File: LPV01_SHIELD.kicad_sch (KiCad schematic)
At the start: 123 parts, among them J1 Screw_Terminal_01x02, J10 SPI_header, J11 Power_socket, J15 Inputs, J16 Screw_Terminal_01x02, J17 Wiegand, J2 Screw_Terminal_01x02, J22 Inputs, J23 Screw_Terminal_01x02, J24 Conn_01x02_Pin, J3 Screw_Terminal_01x02, J9 GPIO_header, Q1 BC817, Q10 BC817, Q11 BC817, Q12 BC817, Q13 BC817, Q14 BC817, Q15 BC817, Q2 BC817, Q3 BC817, Q4 TLP521-4XSM, Q5 TLP521-4XSM, Q6 TLP521-4XSM, Q7 BC817, Q8 TLP521-4XSM, Q9 BC817, SW1 SW_SPST, SW10 SW_SPST, SW11 SW_SPST, SW2 SW_SPST, SW3 SW_SPST, SW4 SW_SPST, SW5 SW_SPST, SW6 SW_SPST, SW7 SW_SPST, SW8 SW_SPST, SW9 SW_SPST, U1 TLP175A, U2 TLP175A, U3 TLP175A

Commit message: PCB rebuilt
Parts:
- removed D10, D12, D14, D8: LED, symbol Device:LED
- removed D18, D20, D22, D24, D26, D28, D29: LED, LED_SMD:LED_0603_1608Metric, symbol Device:LED
- removed D2, D4, D6: SMF48CA, Diode_SMD:D_SMA, symbol Diode:SD36_SOD323
- removed D21, D23, D25, D27, D30, D31: D, symbol Device:D
- removed J1, J2, J3: Screw_Terminal_01x02, TerminalBlock_Phoenix:TerminalBlock_Phoenix_MKDS-1,5-2_1x02_P5.00mm_Horizontal, symbol Connector:Screw_Terminal_01x02
- removed J15: Inputs, TerminalBlock_Phoenix:TerminalBlock_Phoenix_PT-1,5-8-3.5-H_1x08_P3.50mm_Horizontal, symbol Connector:Screw_Terminal_01x08
- removed J16: Screw_Terminal_01x02, TerminalBlock_Phoenix:TerminalBlock_Phoenix_PT-1,5-2-3.5-H_1x02_P3.50mm_Horizontal, symbol Connector:Screw_Terminal_01x02
- removed Q1, Q10, Q11, Q12, Q13, Q14, Q15: BC817, Package_TO_SOT_SMD:SOT-23, symbol Transistor_BJT:BC817
- removed Q4, Q5, Q6, Q8: TLP521-4XSM, SamacSys_Parts:TLP5214XSM, symbol SamacSys_Parts:TLP521-4XSM
- removed R10: 4k7, Resistor_SMD:R_0603_1608Metric, symbol Device:R
- removed R34, R35: 2k2, Resistor_SMD:R_0603_1608Metric, symbol Device:R
- removed R36, R38, R39, R40, R41, R42, R43, R44, R45, R46, R47: 10k, Resistor_SMD:R_0603_1608Metric, symbol Device:R
- removed R37: 10k ->, Resistor_SMD:R_0603_1608Metric, symbol Device:R
- removed R48, R49, R50, R51, R52, R53, R54, R55, R56, R58, R59, R60, R61, R62, R63: 1k, Resistor_SMD:R_0603_1608Metric, symbol Device:R
- removed SW10, SW11, SW9: SW_SPST, Button_Switch_SMD:SW_SPST_CK_RS282G05A3, symbol Switch:SW_SPST
- removed U1, U2, U3: TLP175A, Package_SO:MFSOP6-4_4.4x3.6mm_P1.27mm, symbol Relay_SolidState:TLP175A
- added D10, D12, D14, D4, D6, D8: D, Diode_SMD:D_MicroMELF, symbol Device:D
- added D9: LED, LED_SMD:LED_0603_1608Metric, symbol Device:LED
- added J6: Relay_PWR, TerminalBlock_Phoenix:TerminalBlock_Phoenix_PT-1,5-2-3.5-H_1x02_P3.50mm_Horizontal, symbol Connector:Screw_Terminal_01x02
- added Q101, Q102: TLP521-4XSM, SamacSys_Parts:TLP5214XSM, symbol SamacSys_Parts:TLP521-4XSM
- added Q4, Q5, Q6, Q8: BC817, Package_TO_SOT_SMD:SOT-23, symbol Transistor_BJT:BC817
- added R17, R20, R23, R26: 2k2, Resistor_SMD:R_0603_1608Metric, symbol Device:R
- added R18, R21, R24, R27: 22k, Resistor_SMD:R_0603_1608Metric, symbol Device:R
- added R19, R22, R25: 4k7, Resistor_SMD:R_0603_1608Metric, symbol Device:R
- D11, D13, D15, D7: footprint (none) -> LED_SMD:LED_0603_1608Metric
- D16: footprint (none) -> Diode_SMD:D_MicroMELF
- D17: value LED -> STATUS
- D2: renamed from D19; footprint (none) -> Diode_SMD:D_MicroMELF
- J2: renamed from J11; value Power_socket -> PWR_socket
- J4: renamed from J23; value Screw_Terminal_01x02 -> Relay_PWR_in
- J5: renamed from J24; footprint (none) -> Connector_PinHeader_2.54mm:PinHeader_1x02_P2.54mm_Vertical
- R1, R5: value 1k -> 470R
- R10: renamed from R57; value 1k -> 4k7
- R11: value 4k7 -> 2k2
- R12, R15: value 10k -> 22k
- R13, R16, R28: value 10k -> 4k7
- R2, R3, R6, R7: value 4k7 -> 470R
- R30: value 2k2 -> 22k
- R31: value 2k2 -> 4k7
- R33: value 2k2 -> 1k
- R4, R8: value 10k -> 470R
- R9: value 1k -> 22k
- renumbered J9 to J1, J10 to J3, J17 to J7, J22 to J8, Q9 to Q1
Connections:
- net +24V: no longer R14.2, R29.2, R30.2, R31.2, R32.2, R33.2
- net +5V: now also SW1.2 (B), SW2.2 (B), SW3.2 (B), SW4.2 (B), SW5.2 (B), SW6.2 (B), SW7.2 (B), SW8.2 (B), Q101.10 (C_1), Q101.12 (C_2), Q101.14 (C_3), Q101.16 (C_4), Q102.10 (C_1), Q102.12 (C_2), Q102.14 (C_3), Q102.16 (C_4); no longer R1.2, R13.1, R15.1, R16.1, R2.2, R28.1, R5.2, R6.2, R9.2, SW4.1 (A), SW5.1 (A), SW6.1 (A), SW7.1 (A), SW8.1 (A)
- net D10: now also R1.2
- net D11: now also R2.2
- net D12: now also R3.2
- net D13: now also D17.2 (A)
- net D18: now also R5.2
- net D19: now also R6.2
- net D2: no longer R13.2
- net D21: now also R4.2
- net D22: now also R7.2
- net D23: now also R8.2
- net D3: no longer R15.2
- net D4: no longer R16.2
- net D5: no longer R28.2
- net GND: now also R15.2, R30.2, R33.1, R9.2, Q101.2 (K_1), Q101.4 (K_2), Q101.6 (K_3), Q101.8 (K_4), Q102.2 (K_1), Q102.4 (K_2), Q102.6 (K_3), Q102.8 (K_4), Q4.2 (E), Q5.2 (E), Q6.2 (E), Q8.2 (E), R18.2, R21.2, R24.2, R27.2; no longer R4.2, R8.2, SW1.2 (B), SW2.2 (B), SW3.2 (B)
- net MISO: no longer R3.1
- net MOSI: no longer R11.1
- net O1: now also R10.1, R9.1, SW1.1 (A), Q101.15 (E_4); no longer D17.2 (A), SW4.2 (B), SW5.2 (B), SW6.2 (B), SW7.2 (B), SW8.2 (B)
- net O2: now also R12.1, R13.1, SW2.1 (A), Q101.13 (E_3)
- net O3: now also R15.1, R16.1, SW3.1 (A), Q101.11 (E_2)
- net O4: now also SW4.1 (A), Q101.9 (E_1), R18.1, R19.1
- net O5: now also SW5.1 (A), Q102.15 (E_4), R21.1, R22.1
- net O6: now also SW6.1 (A), Q102.13 (E_3), R24.1, R25.1
- net O7: now also R28.1, SW7.1 (A), Q102.11 (E_2), R27.1
- net O8: now also R30.1, R31.1, SW8.1 (A), Q102.9 (E_1)
- net OUT1: now also D1.1 (K), D2.2 (A), Q1.3 (C); no longer D16.2 (A), Q7.3 (C)
- net OUT2: now also D3.1 (K), Q2.3 (C), D4.2 (A); no longer D2.2 (A), Q1.3 (C)
- net OUT3: now also D5.1 (K), Q3.3 (C), D6.2 (A)
- net OUT4: now also D7.1 (K), D8.2 (A), Q4.3 (C)
- net OUT5: now also D10.2 (A), D9.1 (K), Q5.3 (C)
- net OUT6: now also D11.1 (K), D12.2 (A), Q6.3 (C)
- net OUT7: now also D13.1 (K), Q7.3 (C), D14.2 (A)
- net OUT8: now also D15.1 (K), D16.2 (A), Q8.3 (C)
- net SCK: no longer R7.1
- net VR: now also R11.1, R14.1, R29.1, R32.1, D10.1 (K), D12.1 (K), D14.1 (K), D4.1 (K), D6.1 (K), D8.1 (K), J6.1 (Pin_1), J6.2 (Pin_2), R17.1, R20.1, R23.1, R26.1
- net at R4.1: now also Q101.7 (A_4); no longer R3.2
- net at Q7.1 (B): now also R28.2
- net at D15.2 (A): now also R32.2
- net at D17.1 (K): now also R33.2
- net at D11.2 (A): now also R26.2; no longer R30.1
- net at D5.2 (A): now also R17.2
- net at R6.1: now also Q102.3 (A_2); no longer D3.2 (A)
- net at R5.1: now also Q102.1 (A_1)
- net at R1.1: now also Q101.1 (A_1)
- net at D13.2 (A): now also R29.2; no longer R33.1
- net at D7.2 (A): now also R20.2; no longer R14.1
- net at R2.1: now also Q101.3 (A_2); no longer D1.2 (A)
- new net: Q6.1 (B), R25.2
- new net: Q8.1 (B), R31.2
- new net: D9.2 (A), R23.2
- new net: Q4.1 (B), R19.2
- new net: Q5.1 (B), R22.2
- new net: Q102.7 (A_4), R8.1
- new net: Q3.1 (B), R16.2
- new net: D1.2 (A), R11.2
- new net: Q101.5 (A_3), R3.1
- new net: Q102.5 (A_3), R7.1
- new net: D3.2 (A), R14.2
- new net: Q2.1 (B), R13.2
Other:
- removed sheet USART
- removed sheet USB_hub
- added sheet Inputs (inputs.kicad_sch)
- moved on the sheet: D2, J1, J2, J3, J4, J5, J7, J8, Q1, R10

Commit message: First traces added
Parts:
- added H1, H2, H3, H4: MountingHole, MountingHole:MountingHole_3.2mm_M3_DIN965_Pad, symbol Mechanical:MountingHole
- D10, D12, D14, D16, D2, D4, D6, D8: footprint Diode_SMD:D_MicroMELF -> Diode_SMD:D_SMA
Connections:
- net +5V: now also Q101.11 (E_2), Q101.13 (E_3), Q101.15 (E_4), Q101.9 (E_1), Q102.11 (E_2), Q102.13 (E_3), Q102.15 (E_4), Q102.9 (E_1); no longer Q101.10 (C_1), Q101.12 (C_2), Q101.14 (C_3), Q101.16 (C_4), Q102.10 (C_1), Q102.12 (C_2), Q102.14 (C_3), Q102.16 (C_4)
- net D10: no longer R1.2
- net D11: no longer R2.2
- net D12: no longer R3.2
- net D18: no longer R5.2
- net D19: no longer R6.2
- net D21: no longer R4.2
- net D22: no longer R7.2
- net D23: no longer R8.2
- net GND: now also Q101.1 (A_1), Q101.3 (A_2), Q101.5 (A_3), Q101.7 (A_4), Q102.1 (A_1), Q102.3 (A_2), Q102.5 (A_3), Q102.7 (A_4); no longer Q101.2 (K_1), Q101.4 (K_2), Q101.6 (K_3), Q101.8 (K_4), Q102.2 (K_1), Q102.4 (K_2), Q102.6 (K_3), Q102.8 (K_4)
- net O1: now also Q101.10 (C_1); no longer Q101.15 (E_4)
- net O2: now also Q101.12 (C_2); no longer Q101.13 (E_3)
- net O3: now also Q101.14 (C_3); no longer Q101.11 (E_2)
- net O4: now also Q101.16 (C_4); no longer Q101.9 (E_1)
- net O5: now also Q102.10 (C_1); no longer Q102.15 (E_4)
- net O6: now also Q102.12 (C_2); no longer Q102.13 (E_3)
- net O7: now also Q102.14 (C_3); no longer Q102.11 (E_2)
- net O8: now also Q102.16 (C_4); no longer Q102.9 (E_1)
- net at R6.1: now also Q102.6 (K_3); no longer Q102.3 (A_2)
- net at R8.1: now also Q102.2 (K_1); no longer Q102.7 (A_4)
- net at R2.1: now also Q101.6 (K_3); no longer Q101.3 (A_2)
- net at R3.1: now also Q101.4 (K_2); no longer Q101.5 (A_3)
- net at R7.1: now also Q102.4 (K_2); no longer Q102.5 (A_3)
- net at R4.1: now also Q101.2 (K_1); no longer Q101.7 (A_4)
- net at R5.1: now also Q102.8 (K_4); no longer Q102.1 (A_1)
- net at R1.1: now also Q101.8 (K_4); no longer Q101.1 (A_1)

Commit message: More traces + components alignment
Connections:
- net +5V: now also Q101.10 (C_1), Q101.12 (C_2), Q101.14 (C_3), Q101.16 (C_4), Q102.10 (C_1), Q102.12 (C_2), Q102.14 (C_3), Q102.16 (C_4); no longer Q101.11 (E_2), Q101.13 (E_3), Q101.15 (E_4), Q101.9 (E_1), Q102.11 (E_2), Q102.13 (E_3), Q102.15 (E_4), Q102.9 (E_1)
- net D10: now also R5.2
- net D11: now also R7.2
- net D2: now also R2.2
- net D3: now also R4.2
- net D4: now also R6.2
- net D5: now also R8.2
- net D8: now also R1.2
- net D9: now also R3.2
- net GND: now also Q101.2 (K_1), Q101.4 (K_2), Q101.6 (K_3), Q101.8 (K_4), Q102.2 (K_1), Q102.4 (K_2), Q102.6 (K_3), Q102.8 (K_4); no longer Q101.1 (A_1), Q101.3 (A_2), Q101.5 (A_3), Q101.7 (A_4), Q102.1 (A_1), Q102.3 (A_2), Q102.5 (A_3), Q102.7 (A_4)
- net O1: now also Q101.15 (E_4); no longer Q101.10 (C_1)
- net O2: now also Q101.13 (E_3); no longer Q101.12 (C_2)
- net O3: now also Q101.11 (E_2); no longer Q101.14 (C_3)
- net O4: now also Q101.9 (E_1); no longer Q101.16 (C_4)
- net O5: now also Q102.15 (E_4); no longer Q102.10 (C_1)
- net O6: now also Q102.13 (E_3); no longer Q102.12 (C_2)
- net O7: now also Q102.11 (E_2); no longer Q102.14 (C_3)
- net O8: now also Q102.9 (E_1); no longer Q102.16 (C_4)
- net at R6.1: now also Q102.3 (A_2); no longer Q102.6 (K_3)
- net at R8.1: now also Q102.7 (A_4); no longer Q102.2 (K_1)
- net at R2.1: now also Q101.3 (A_2); no longer Q101.6 (K_3)
- net at R3.1: now also Q101.5 (A_3); no longer Q101.4 (K_2)
- net at R7.1: now also Q102.5 (A_3); no longer Q102.4 (K_2)
- net at R4.1: now also Q101.7 (A_4); no longer Q101.2 (K_1)
- net at R5.1: now also Q102.1 (A_1); no longer Q102.8 (K_4)
- net at R1.1: now also Q101.1 (A_1); no longer Q101.8 (K_4)
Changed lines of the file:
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@@
 		)
 	)
-	(global_label "D23"
+	(global_label "D9"
 		(shape input)
-		(at 21.59 73.66 180)
+		(at 22.86 36.83 180)
 		(fields_autoplaced yes)
 		(effects
@@
 		)
 		(property "Intersheetrefs" "${INTERSHEET_REFS}"
-			(at 14.9158 73.66 0)
+			(at 17.3953 36.83 0)
 			(effects
 				(font
@@
 		)
 	)
-	(global_label "D18"
+	(global_label "D4"
 		(shape input)
-		(at 21.59 58.42 180)
+		(at 22.86 63.5 180)
 		(fields_autoplaced yes)
 		(effects
@@
 		)
 		(property "Intersheetrefs" "${INTERSHEET_REFS}"
-			(at 14.9158 58.42 0)
+			(at 17.3953 63.5 0)
 			(effects
 				(font
@@
 		)
 	)
-	(global_label "D11"
+	(global_label "D8"
 		(shape input)
-		(at 21.59 31.75 180)
+		(at 22.86 26.67 180)
 		(fields_autoplaced yes)
 		(effects
@@
 		)
 		(property "Intersheetrefs" "${INTERSHEET_REFS}"
-			(at 14.9158 31.75 0)
+			(at 17.3953 26.67 0)
 			(effects
 				(font
@@
 		)
 	)
-	(global_label "D22"
+	(global_label "D5"
 		(shape input)
-		(at 21.59 68.58 180)
+		(at 22.86 73.66 180)
 		(fields_autoplaced yes)
 		(effects
@@
 		)
 		(property "Intersheetrefs" "${INTERSHEET_REFS}"
-			(at 14.9158 68.58 0)
+			(at 17.3953 73.66 0)
 			(effects
 				(font
@@
 		)
 	)
-	(global_label "D12"
+	(global_label "D3"
 		(shape input)
-		(at 21.59 36.83 180)
+		(at 22.86 41.91 180)
 		(fields_autoplaced yes)
 		(effects
@@
 		)
 		(property "Intersheetrefs" "${INTERSHEET_REFS}"
-			(at 14.9158 36.83 0)
+			(at 17.3953 41.91 0)
 			(effects
 				(font
@@
 		)
 	)
-	(global_label "D19"
+	(global_label "D11"
 		(shape input)
-		(at 21.59 63.5 180)
+		(at 22.86 68.58 180)
 		(fields_autoplaced yes)
 		(effects
@@
 		)
 		(property "Intersheetrefs" "${INTERSHEET_REFS}"
-			(at 14.9158 63.5 0)
+			(at 16.1858 68.58 0)
 			(effects
 				(font
@@
 		)
 	)
-	(global_label "D10"
+	(global_label "D2"
 		(shape input)
-		(at 21.59 26.67 180)
+		(at 22.86 31.75 180)
 		(fields_autoplaced yes)
 		(effects
@@
 		)
 		(property "Intersheetrefs" "${INTERSHEET_REFS}"
-			(at 14.9158 26.67 0)
+			(at 17.3953 31.75 0)
 			(effects
 				(font
@@
 		)
 	)
-	(global_label "D21"
+	(global_label "D10"
 		(shape input)
-		(at 21.59 41.91 180)
+		(at 22.86 58.42 180)
 		(fields_autoplaced yes)
 		(effects
@@
 		)
 		(property "Intersheetrefs" "${INTERSHEET_REFS}"
-			(at 14.9158 41.91 0)
+			(at 16.1858 58.42 0)
 			(effects
 				(font
@@
 	(symbol
 		(lib_id "SamacSys_Parts:TLP521-4XSM")
-		(at 41.91 76.2 0)
-		(mirror x)
+		(at 41.91 58.42 0)
 		(unit 1)
 		(exclude_from_sim no)
@@
 		(dnp no)
 		(property "Reference" "Q102"
-			(at 55.118 51.816 0)
+			(at 55.118 52.07 0)
 			(effects
 				(font
@@
 		)
 		(property "Value" "TLP521-4XSM"
-			(at 54.61 54.356 0)
+			(at 54.864 54.61 0)
 			(effects
 				(font
@@
 		)
 		(property "Footprint" "SamacSys_Parts:TLP5214XSM"
-			(at 63.5 78.74 0)
+			(at 63.5 55.88 0)
 			(effects
 				(font
@@
 		)
 		(property "Datasheet" "http://isocom.com/wp-content/uploads/2018/03/dd93208-small-tlp521-1_2-4-240817.pdf"
-			(at 63.5 76.2 0)
+			(at 63.5 58.42 0)
 			(effects
 				(font
@@
 		)
 		(property "Description" "OPTOISO 5.3KV 4CH TRANS 16SMD"
-			(at 41.91 76.2 0)
+			(at 41.91 58.42 0)
 			(effects
 				(font
@@
 		)
 		(property "Description_1" "OPTOISO 5.3KV 4CH TRANS 16SMD"
-			(at 63.5 73.66 0)
+			(at 63.5 60.96 0)
 			(effects
 				(font
@@
 		)
 		(property "Height" "4.6"
-			(at 63.5 71.12 0)
+			(at 63.5 63.5 0)
 			(effects
 				(font
@@
 		)
 		(property "Manufacturer_Name" "Isocom"
-			(at 63.5 68.58 0)
+			(at 63.5 66.04 0)
 			(effects
 				(font
@@
 		)
 		(property "Manufacturer_Part_Number" "TLP521-4XSM"
-			(at 63.5 66.04 0)
+			(at 63.5 68.58 0)
 			(effects
 				(font
@@
 		)
 		(property "Mouser Part Number" ""
-			(at 63.5 63.5 0)
+			(at 63.5 71.12 0)
 			(effects
 				(font
@@
 		)
 		(property "Mouser Price/Stock" ""
-			(at 63.5 60.96 0)
+			(at 63.5 73.66 0)
 			(effects
 				(font
@@
 		)
 		(property "Arrow Part Number" ""
-			(at 63.5 58.42 0)
+			(at 63.5 76.2 0)
 			(effects
 				(font
@@
 		)
 		(property "Arrow Price/Stock" ""
-			(at 63.5 55.88 0)
+			(at 63.5 78.74 0)
 			(effects
 				(font
@@
 	(symbol
 		(lib_id "SamacSys_Parts:TLP521-4XSM")
-		(at 41.91 44.45 0)
-		(mirror x)
+		(at 41.91 26.67 0)
 		(unit 1)
 		(exclude_from_sim no)
@@
 		)
 		(property "Value" "TLP521-4XSM"
-			(at 54.356 22.098 0)
+			(at 54.864 22.352 0)
 			(effects
 				(font
@@
 		)
 		(property "Footprint" "SamacSys_Parts:TLP5214XSM"
-			(at 63.5 46.99 0)
+			(at 63.5 24.13 0)
 			(effects
 				(font
@@
 		)
 		(property "Datasheet" "http://isocom.com/wp-content/uploads/2018/03/dd93208-small-tlp521-1_2-4-240817.pdf"
-			(at 63.5 44.45 0)
+			(at 63.5 26.67 0)
 			(effects
 				(font
@@
 		)
 		(property "Description" "OPTOISO 5.3KV 4CH TRANS 16SMD"
-			(at 41.91 44.45 0)
+			(at 41.91 26.67 0)
 			(effects
 				(font
@@
 		)
 		(property "Description_1" "OPTOISO 5.3KV 4CH TRANS 16SMD"
-			(at 63.5 41.91 0)
+			(at 63.5 29.21 0)
 			(effects
 				(font
@@
 		)
 		(property "Height" "4.6"
-			(at 63.5 39.37 0)
+			(at 63.5 31.75 0)
 			(effects
 				(font
@@
 		)
 		(property "Manufacturer_Name" "Isocom"
-			(at 63.5 36.83 0)
+			(at 63.5 34.29 0)
 			(effects
 				(font
@@
 		)
 		(property "Manufacturer_Part_Number" "TLP521-4XSM"
-			(at 63.5 34.29 0)
+			(at 63.5 36.83 0)
 			(effects
 				(font
@@
 		)
 		(property "Mouser Part Number" ""
-			(at 63.5 31.75 0)
+			(at 63.5 39.37 0)
 			(effects
 				(font
@@
 		)
 		(property "Mouser Price/Stock" ""
-			(at 63.5 29.21 0)
+			(at 63.5 41.91 0)
 			(effects
 				(font
@@
 		)
 		(property "Arrow Part Number" ""
-			(at 63.5 26.67 0)
+			(at 63.5 44.45 0)
 			(effects
 				(font
@@
 		)
 		(property "Arrow Price/Stock" ""
-			(at 63.5 24.13 0)
+			(at 63.5 46.99 0)
 			(effects
 				(font

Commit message: Made the PCK the size of the LP board
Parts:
- removed Q101, Q102: TLP521-4XSM, SamacSys_Parts:TLP5214XSM, symbol SamacSys_Parts:TLP521-4XSM
- removed SW1, SW2, SW3, SW4, SW5, SW6, SW7, SW8: SW_SPST, Button_Switch_SMD:SW_SPST_CK_RS282G05A3, symbol Switch:SW_SPST
- added U2, U3: TCMT4100, Package_SO:SOP-16_4.4x10.4mm_P1.27mm, symbol Isolator:TCMT4100
- H1, H2, H3, H4: footprint MountingHole:MountingHole_3.2mm_M3_DIN965_Pad -> MountingHole:MountingHole_3.2mm_M3_DIN965
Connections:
- net +5V: now also U2.10, U2.12, U2.14, U2.16, U3.10, U3.12, U3.14, U3.16
- net GND: now also U2.2, U2.4, U2.6, U2.8, U3.2, U3.4, U3.6, U3.8
- net O1: now also U2.15
- net O2: now also U2.13
- net O3: now also U2.11
- net O4: now also U2.9
- net O5: now also U3.15
- net O6: now also U3.13
- net O7: now also U3.11
- net O8: now also U3.9
- net at R6.1: now also U3.3
- net at R8.1: now also U3.7
- net at R2.1: now also U2.3
- net at R3.1: now also U2.5
- net at R7.1: now also U3.5
- net at R4.1: now also U2.7
- net at R5.1: now also U3.1
- net at R1.1: now also U2.1
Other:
- moved on the sheet: D17, H1, H2, H3, H4, J1, J2, J3, J4, J5, J6, J7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

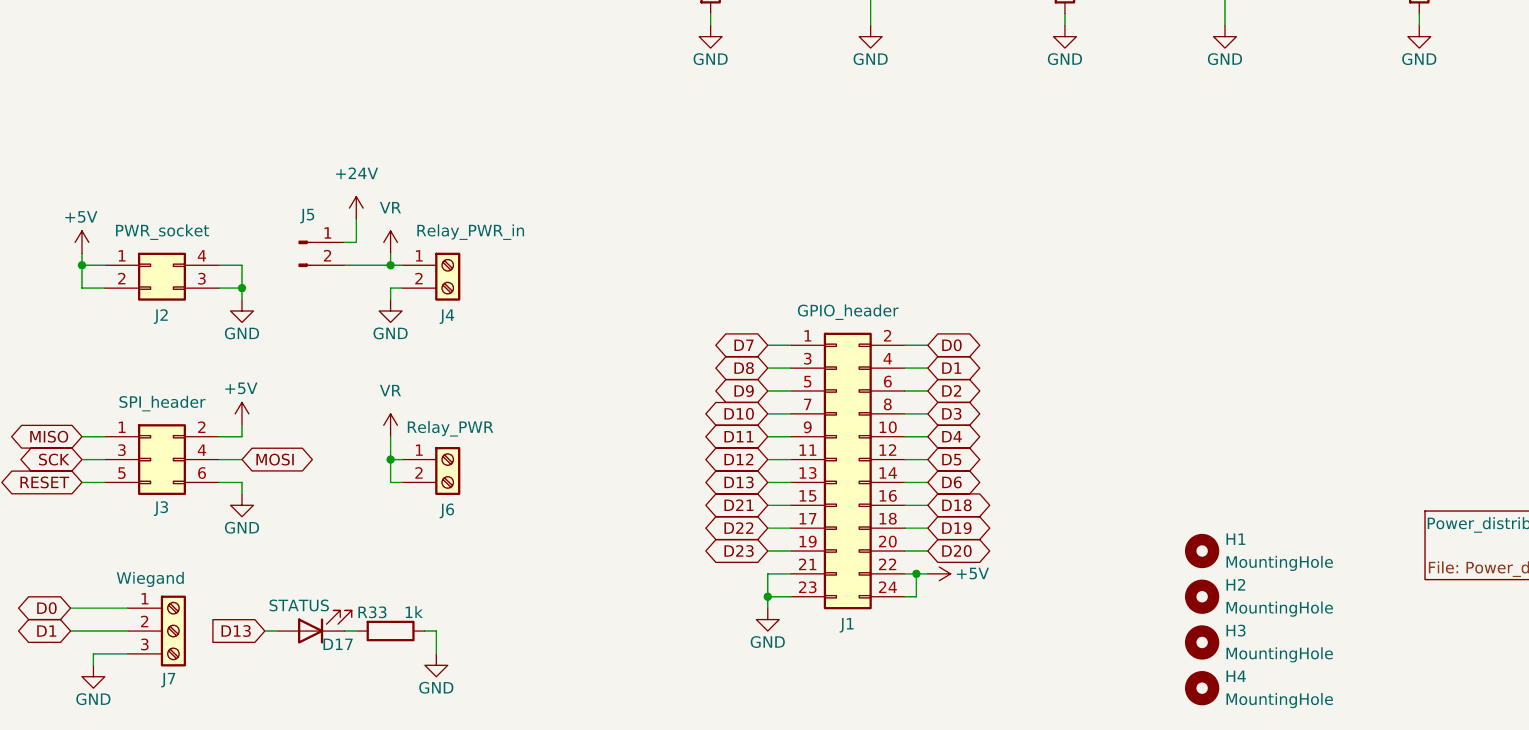
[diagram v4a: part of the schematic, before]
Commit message: PCB shortened to final measurements
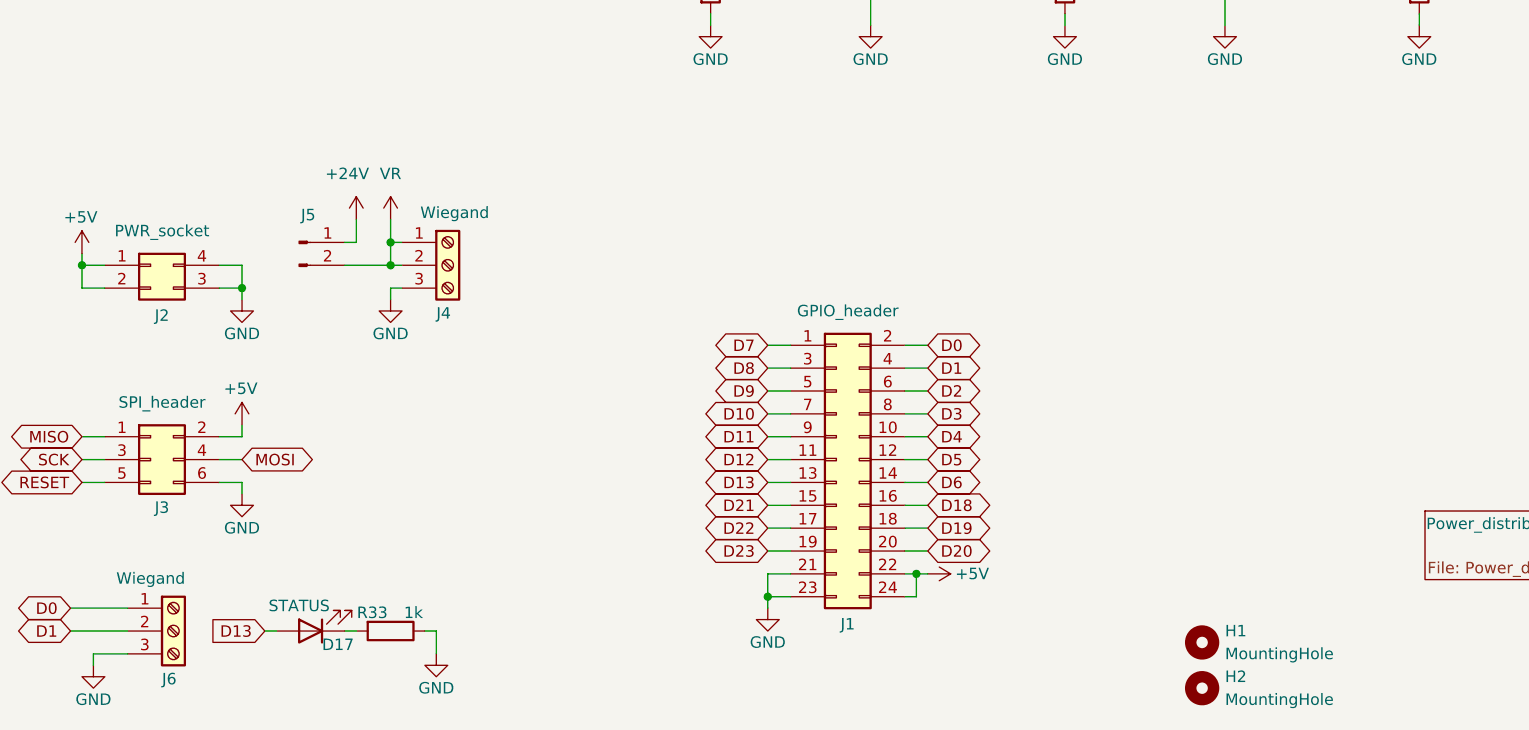
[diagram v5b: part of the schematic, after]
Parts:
- removed H1, H2: MountingHole, MountingHole:MountingHole_3.2mm_M3_DIN965, symbol Mechanical:MountingHole
- removed J4: Relay_PWR_in, TerminalBlock_Phoenix:TerminalBlock_Phoenix_PT-1,5-2-3.5-H_1x02_P3.50mm_Horizontal, symbol Connector:Screw_Terminal_01x02
- removed J6: Relay_PWR, TerminalBlock_Phoenix:TerminalBlock_Phoenix_PT-1,5-2-3.5-H_1x02_P3.50mm_Horizontal, symbol Connector:Screw_Terminal_01x02
- added J4: Wiegand, TerminalBlock_Phoenix:TerminalBlock_Phoenix_PT-1,5-3-3.5-H_1x03_P3.50mm_Horizontal, symbol Connector:Screw_Terminal_01x03
- renumbered H3 to H1, H4 to H2, J7 to J6
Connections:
- net GND: now also J4.3 (Pin_3)
- net VR: now also J4.1 (Pin_1), J4.2 (Pin_2)
